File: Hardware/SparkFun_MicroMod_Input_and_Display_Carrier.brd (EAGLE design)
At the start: 57.1 x 82.5 mm, 107 parts, among them J1 MICROMOD-2222-C, J2 MICRO-SD, J3 USB-C_Prog, J4 AVR_SPI_PROG_3X2TESTPOINTS, J5 2.4" TFT, J6 QWIIC_RA, J7 CORTEX_JTAG_DEBUG, Q1 1.1A/600mΩ, Q2 600mA/40V, U2 ATTINY84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

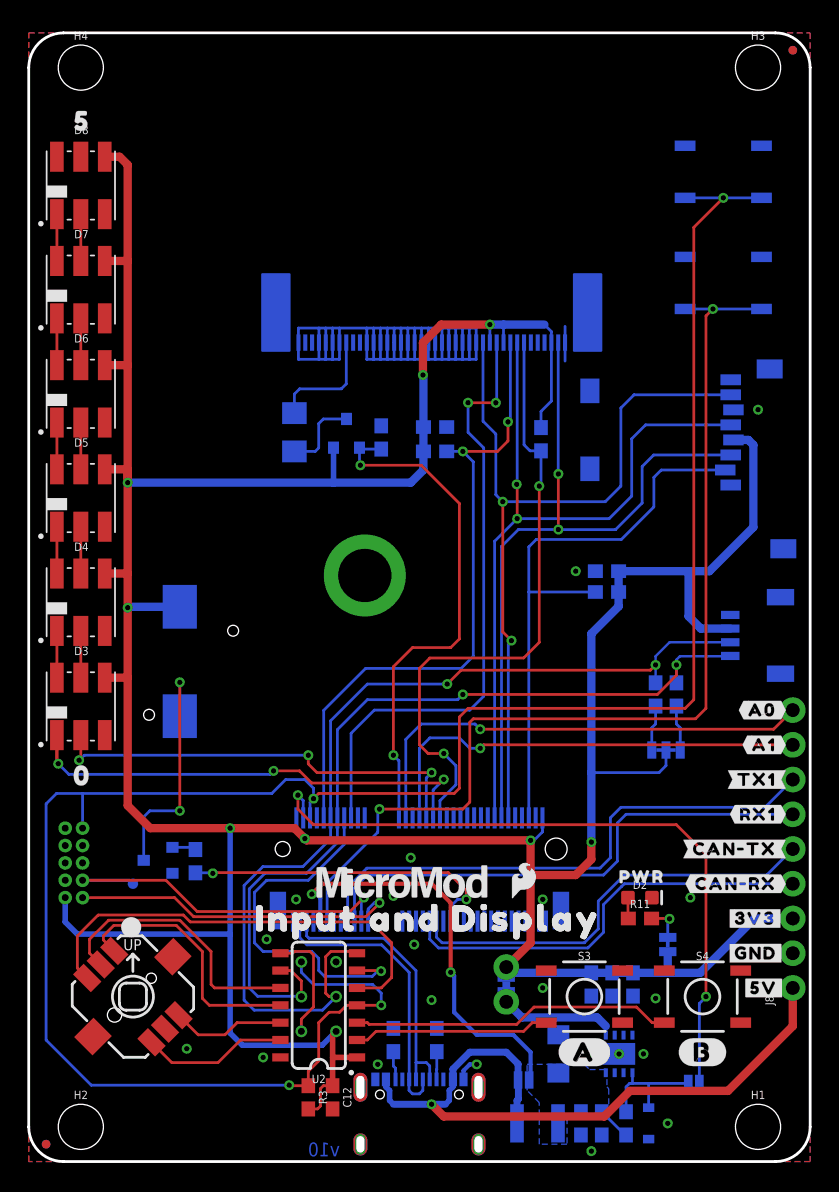
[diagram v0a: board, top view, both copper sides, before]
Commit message: v11
Updated MM conenctor SPI pins
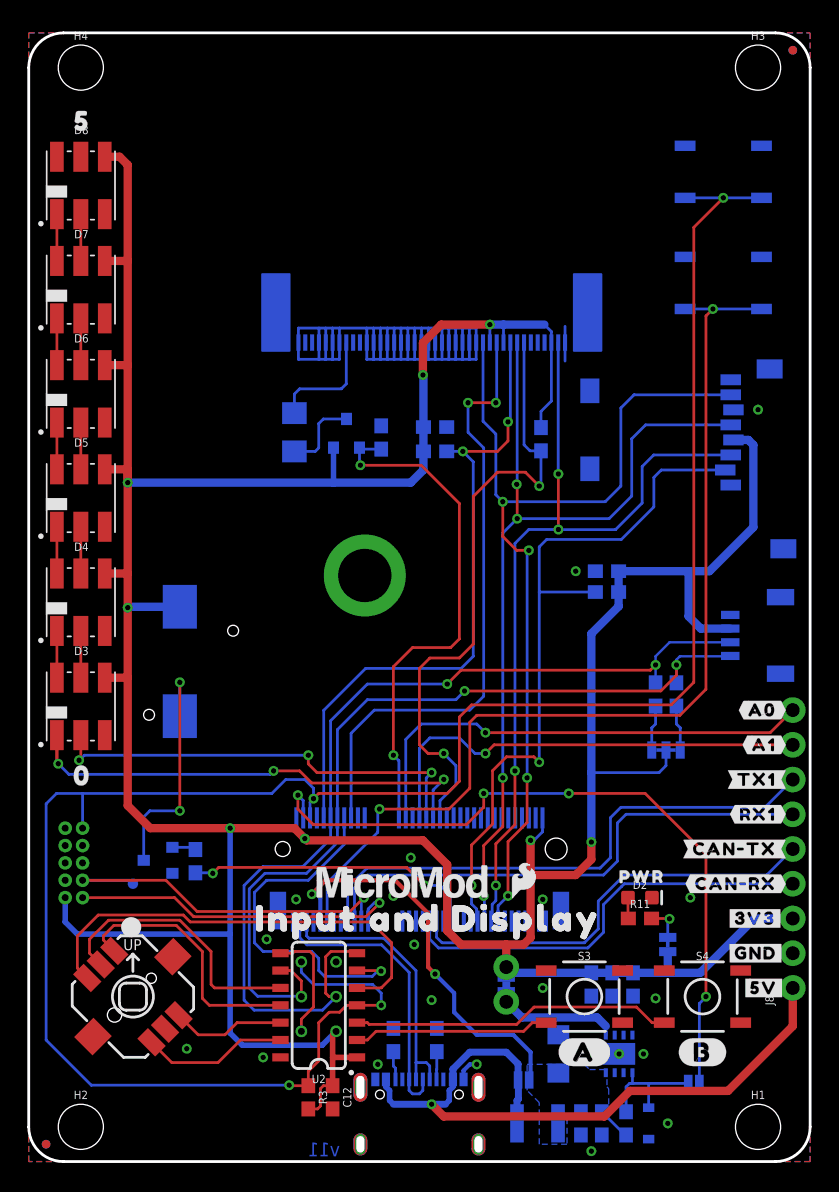
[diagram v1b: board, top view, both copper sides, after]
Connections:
- net !SD_CS: now also J1.55; no longer J1.70
- net SPI_CIPO: now also J1.61; no longer J1.64
- net SPI_COPI: now also J1.59; no longer J1.62
- net SPI_SCK: now also J1.57; no longer J1.60
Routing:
- net !SD_CS: track 42.6 -> 52.9 mm, vias 0 -> 2
- net SPI_CIPO: track 59.0 -> 68.4 mm, vias 2 -> 4
- net SPI_SCK: track 56.4 -> 64.3 mm, vias 2 -> 4
- net SPI_COPI: track 54.6 -> 62.1 mm, vias 2 -> 4
- net 3.3V: track 291.7 -> 296.6 mm
- net 3.3V_EN: track 51.0 -> 53.5 mm, vias 2 -> 4
- net BUZZER: track 23.5 -> 21.6 mm
- net !BOOT: track 75.1 -> 73.7 mm
- net VIN: track 33.0 -> 31.8 mm
- net !RESET: track 158.4 -> 157.4 mm
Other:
- board text added: "v11"
- board text removed: "v10"
